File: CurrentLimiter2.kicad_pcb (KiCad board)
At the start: 2 copper layers, 55 x 20 mm, 10 parts, among them J1 Screw_Terminal_01x02, J2 Screw_Terminal_01x02, Q1 BCP54, Q2 MJD112

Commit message: v2 wersja wyslana do Elpinu do wykonania i zmontowania w Blaberk
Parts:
- removed JP1: SolderJumper_2_Open, Jumper:SolderJumper-2_P1.3mm_Open_RoundedPad1.0x1.5mm
- removed R4: R, Resistor_SMD:R_1206_3216Metric_Pad1.30x1.75mm_HandSolder
- Q2: footprint Package_TO_SOT_SMD:TO-263-2 -> Package_TO_SOT_SMD:TO-252-3_TabPin2
- R1: value 5k -> 7k15
- R2: value R -> 20m
- R3: value R -> 470m; footprint Resistor_SMD:R_1206_3216Metric_Pad1.30x1.75mm_HandSolder -> Resistor_SMD:R_2010_5025Metric_Pad1.40x2.65mm_HandSolder
- moved R2 5.50 mm to (127.5, 93.0)
- moved R1 2.24 mm to (140.0, 93.0), turned to 180 degrees
- moved R3 1.12 mm to (122.5, 94.5), turned to -90 degrees
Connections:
- Q1 pad 1: Net-(J1-Pin_2) -> Net-(Q1-E)
- Q1 pad 3: Net-(JP1-A) -> Net-(J1-Pin_2)
- Q2 pad 3: Net-(JP1-A) -> Net-(Q1-E)
- R2 pad 1: Net-(JP1-B) -> Net-(Q1-E)
- R2 pad 2: Net-(J1-Pin_2) -> Net-(R2-Pad2)
- R3 pad 1: Net-(JP1-B) -> Net-(R2-Pad2)
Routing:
- net Net-(Q1-E): track 0.00 -> 28.0 mm, vias 0 -> 2
- net Net-(JP1-A): track 25.6 -> 0.00 mm, vias 2 -> 0
- net Net-(JP1-B): track 13.8 -> 0.00 mm, vias 1 -> 0
- net Net-(Q1-C): track 44.9 -> 40.3 mm
- net Net-(R2-Pad2): track 0.00 -> 3.82 mm
- net Net-(J1-Pin_1): track 58.1 -> 59.9 mm
- net Net-(J1-Pin_2): track 25.8 -> 26.9 mm
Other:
- board text added: "CurrLim2v2"
- board text removed: "CurrLim2"

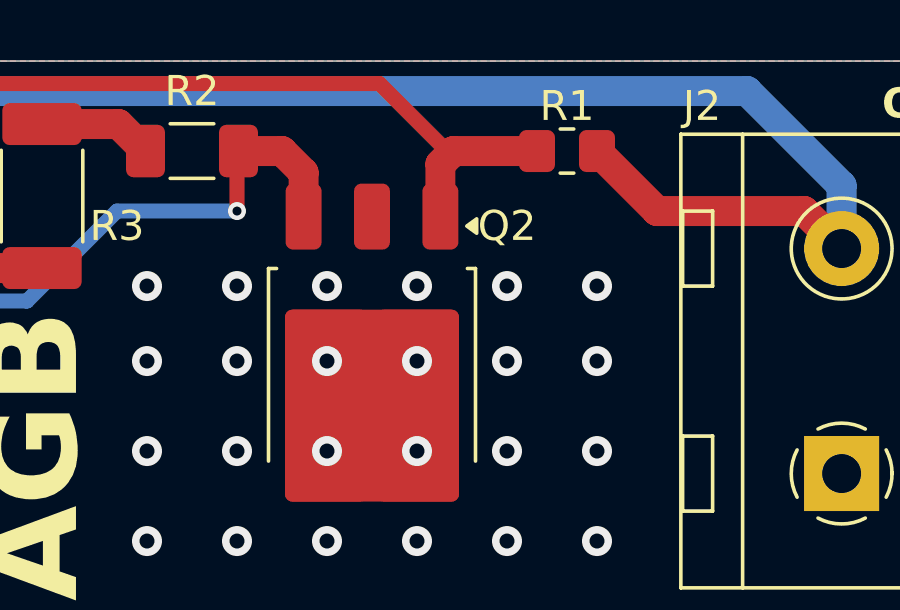
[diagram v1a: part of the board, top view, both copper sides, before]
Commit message: zmieniona podstawka Darlingtona na 2 pinowa
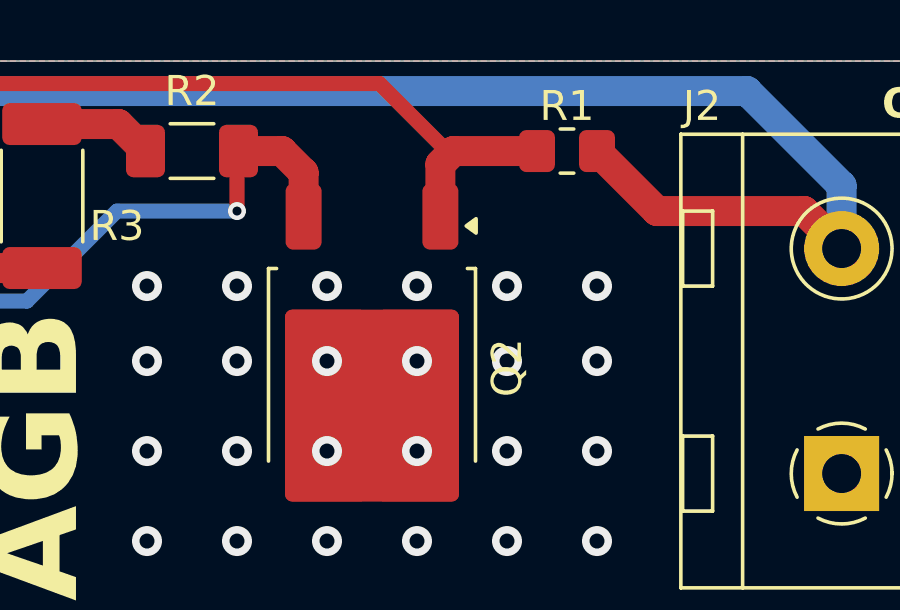
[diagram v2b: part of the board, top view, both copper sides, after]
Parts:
- Q2: footprint Package_TO_SOT_SMD:TO-252-3_TabPin2 -> Package_TO_SOT_SMD:TO-252-2
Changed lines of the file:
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@@
 		)
 	)
-	(footprint "Package_TO_SOT_SMD:TO-252-3_TabPin2"
+	(footprint "Package_TO_SOT_SMD:TO-252-2"
 		(layer "F.Cu")
 		(at 133.5 100.225 -90)
@@
 		(tags "DPAK TO-252 DPAK-3 TO-252-3 SOT-428")
 		(property "Reference" "Q2"
-			(at -4.725 -4.5 180)
+			(at 0 -4.5 -90)
 			(layer "F.SilkS")
 			(effects
@@
 		)
 		(property "Value" "MJD112"
-			(at 0 4.5 90)
-			(layer "F.Fab")
-			(hide yes)
+			(at 0 4.5 -90)
+			(layer "F.Fab")
 			(effects
 				(font
@@
 			)
 		)
-		(property "Footprint" "Package_TO_SOT_SMD:TO-252-3_TabPin2"
+		(property "Footprint" "Package_TO_SOT_SMD:TO-252-2"
 			(at 0 0 -90)
 			(unlocked yes)
@@
 		(fp_poly
 			(pts
-				(xy -4.725 -3.16) (xy -4.965 -3.49) (xy -4.485 -3.49) (xy -4.725 -3.16)
+				(xy -4.73 -3.14) (xy -4.97 -3.47) (xy -4.49 -3.47) (xy -4.73 -3.14)
 			)
 			(stroke
@@
 		)
 		(fp_line
-			(start -5.81 0.375)
-			(end -3.11 0.375)
-			(stroke
-				(width 0.1)
-				(type solid)
-			)
-			(layer "F.Fab")
-		)
-		(fp_line
-			(start -5.81 -0.375)
-			(end -5.81 0.375)
-			(stroke
-				(width 0.1)
-				(type solid)
-			)
-			(layer "F.Fab")
-		)
-		(fp_line
-			(start -3.11 -0.375)
-			(end -5.81 -0.375)
-			(stroke
-				(width 0.1)
-				(type solid)
-			)
-			(layer "F.Fab")
-		)
-		(fp_line
 			(start -5.81 -1.905)
 			(end -3.11 -1.905)
@@
 		)
 		(fp_text user "${REFERENCE}"
-			(at 0 0 90)
+			(at 0 0 -90)
 			(layer "F.Fab")
 			(effects
@@
 		)
 		(pad "2" smd roundrect
-			(at -5.04 0 270)
-			(size 2.2 1.2)
-			(layers "F.Cu" "F.Paste" "F.Mask")
-			(roundrect_rratio 0.208333)
-			(net 4 "/Col")
-			(pinfunction "C")
-			(pintype "passive")
-		)
-		(pad "2" smd roundrect
 			(at -0.415 -1.525 270)
 			(size 3.05 2.75)
@@
 			(pintype "passive")
 		)
-		(model "${KICAD8_3DMODEL_DIR}/Package_TO_SOT_SMD.3dshapes/TO-252-3_TabPin2.wrl"
+		(model "${KICAD8_3DMODEL_DIR}/Package_TO_SOT_SMD.3dshapes/TO-252-2.wrl"
 			(offset
 				(xyz 0 0 0)
